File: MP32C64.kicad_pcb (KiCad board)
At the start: 2 copper layers, 14 parts, among them CN2 C64_CASS_PORT, SW1 SW_SPDT, U1 4069

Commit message: Almost ready
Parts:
- added CN1: AUDIO_IN, MP32C64:SWITCHCRAFT_PJRAN1X1U01X, F.Cu at (155.1, 94.7)
- R1, R2, R3, R4, R5, R6, R7, R8: footprint Resistor_THT:R_Axial_DIN0207_L6.3mm_D2.5mm_P7.62mm_Horizontal -> Resistor_THT:R_Axial_DIN0207_L6.3mm_D2.5mm_P10.16mm_Horizontal
- SW1: value SW_SPDT -> SW_INVERT
- U1: value 4069 -> CD4069
- moved SW1 49.3 mm to (136.0, 114.1)
- moved LD1 47.5 mm to (136.0, 98.8), turned to 90 degrees
- moved R7 44.7 mm to (136.0, 109.0), turned to 0 degrees
- moved R6 43.9 mm to (142.4, 91.2), turned to -90 degrees
- moved R8 43.2 mm to (139.8, 91.2), turned to -90 degrees
- moved R5 25.2 mm to (136.0, 106.4), turned to 0 degrees
- moved C2 23.6 mm to (158.9, 114.1), turned to -90 degrees
- moved R3 10.3 mm to (147.4, 101.3)
- moved R2 5.85 mm to (144.9, 101.3)
- moved R4 5.12 mm to (146.2, 103.9)
- moved C1 4.53 mm to (158.9, 109.0)
- moved U1 1.91 mm to (155.1, 112.8)
- moved R1 1.42 mm to (148.7, 103.9)
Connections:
- net /write renamed /write_1
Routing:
- net /motor: track 0.00 -> 35.5 mm, vias 0 -> 1
- net Net-(SW1-C): track 0.00 -> 21.4 mm
- net +5V: track 6.35 -> 26.6 mm, vias 0 -> 1
- net /read: track 13.7 -> 33.0 mm, vias 0 -> 1
- net Net-(R2-Pad1): track 17.3 -> 33.1 mm
- net Net-(R3-Pad1): track 8.67 -> 24.0 mm
- net Net-(SW1-A): track 17.5 -> 32.5 mm
- net Net-(LD1-A1): track 0.00 -> 10.3 mm
- net Net-(SW1-B): track 6.55 -> 14.5 mm
- net Net-(C1-Pad2): track 15.1 -> 21.2 mm
- net Net-(C1-Pad1): track 4.90 -> 10.5 mm
- net Net-(LD1-A2): track 0.00 -> 4.87 mm
- net GND: vias 0 -> 2
- added copper zone on B.Cu, net GND
- added copper zone on F.Cu, net GND
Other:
- board outline added: 31.4 x 41.9 mm
- board text added: "INV"
- board text added: "NORM"

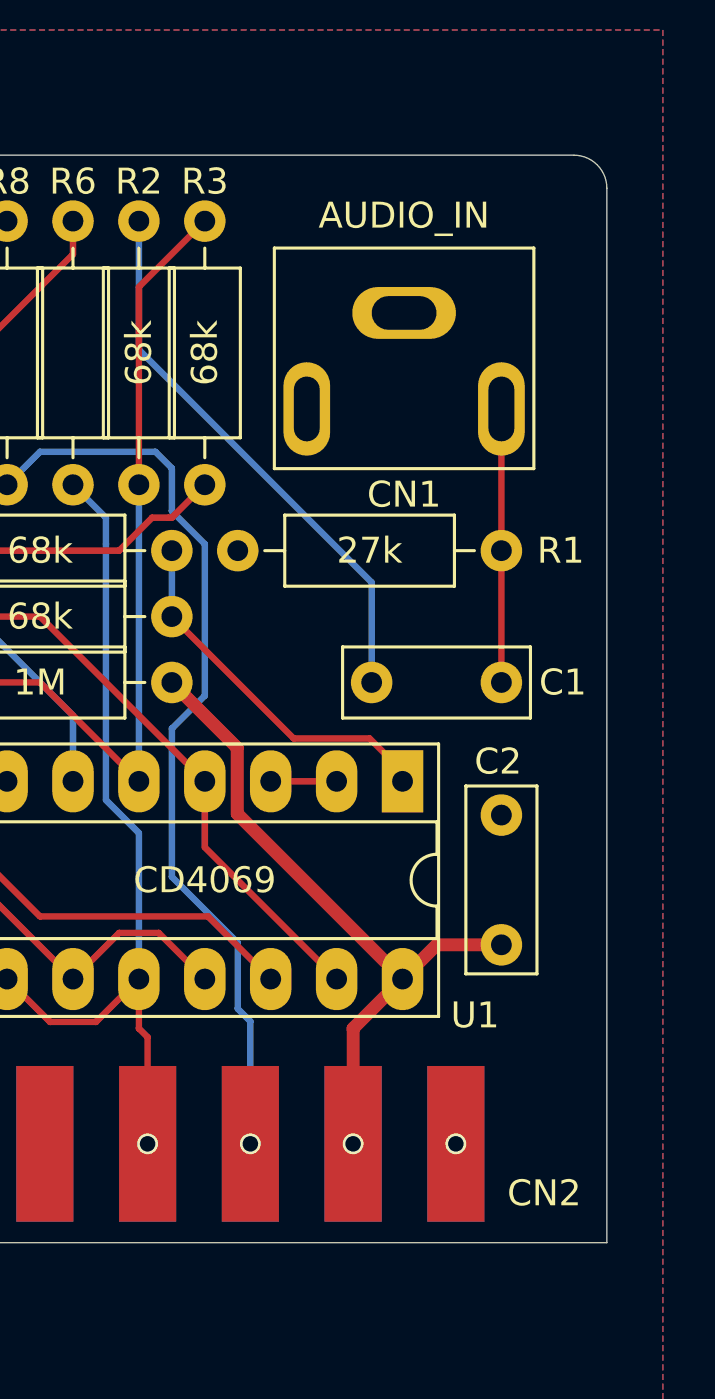
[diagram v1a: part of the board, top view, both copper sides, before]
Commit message: Add dual support for RCA/3.5" jack connector
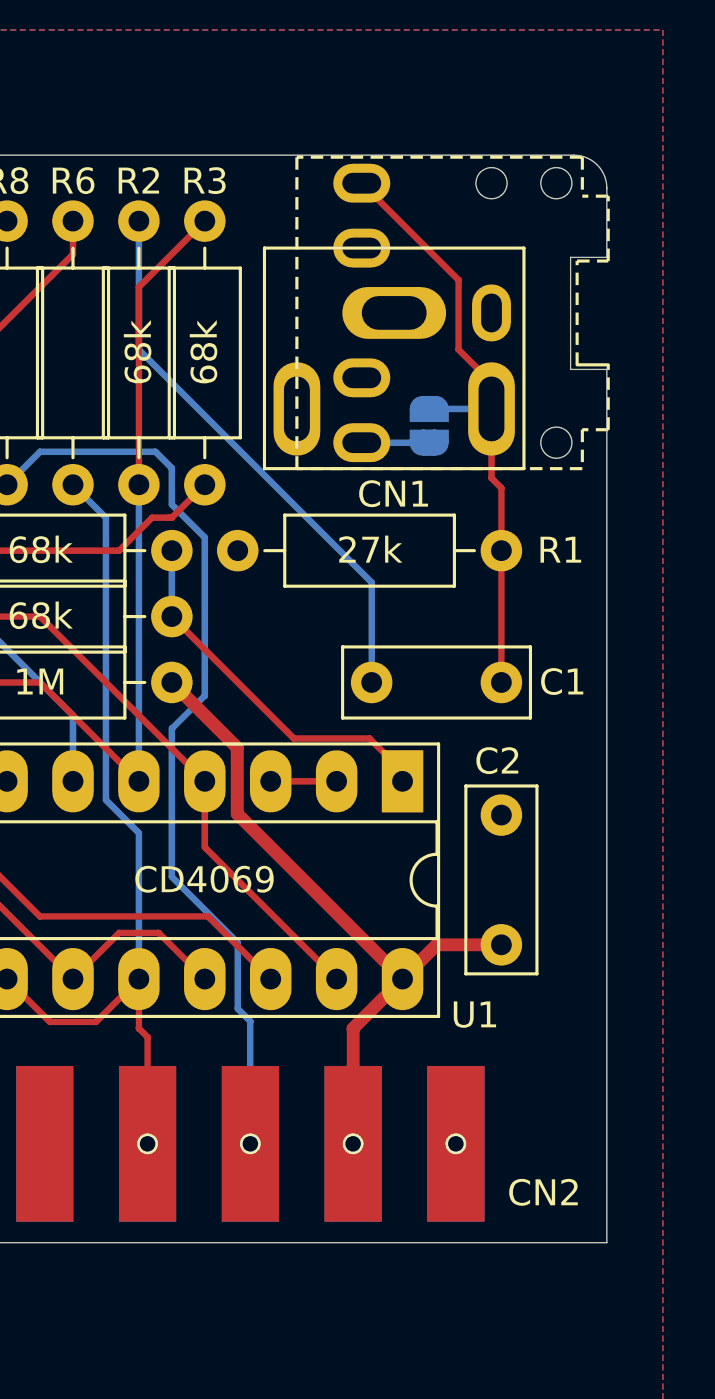
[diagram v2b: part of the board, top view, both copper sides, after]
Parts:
- added CNALT1: JACK_35IN, MP32C64:AudioJack_SJ1-3525N, F.Cu at (158.5, 94.7)
- added JP1: JMP_RING, Jumper:SolderJumper-2_P1.3mm_Open_RoundedPad1.0x1.5mm, B.Cu at (156.1, 99.1)
- moved CN1 0.38 mm to (154.7, 94.7)
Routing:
- net Net-(JP1-A): track 10.5 -> 23.9 mm
- net Net-(JP1-B): track 0.00 -> 2.63 mm
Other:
- outline, holes or cut-outs redrawn

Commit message: Add license, etc.
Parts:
- removed JP1: JMP_RING, Jumper:SolderJumper-2_P1.3mm_Open_RoundedPad1.0x1.5mm
- added V0: LICENSE, MP32C64:cc_by_nc_sa_small, B.Cu at (144.9, 94.3)
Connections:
- net /write_1 renamed /write
- CNALT1 pad R: Net-(JP1-B) -> unconnected-(CNALT1-PadR)
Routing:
- net Net-(JP1-B): track 2.63 -> 0.00 mm
- net Net-(C1-Pad1): track 23.9 -> 21.5 mm
- net /write: vias 0 -> 1
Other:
- board size 31.4 x 41.9 mm -> 31.4 x 41.8 mm
- board text added: "MP32C64 CC-BY-NC-SA"
- board text added: "Original design by Kopsec"
- board text added: "V1"
- board text added: "github.com/SukkoPera/ MP32C64"

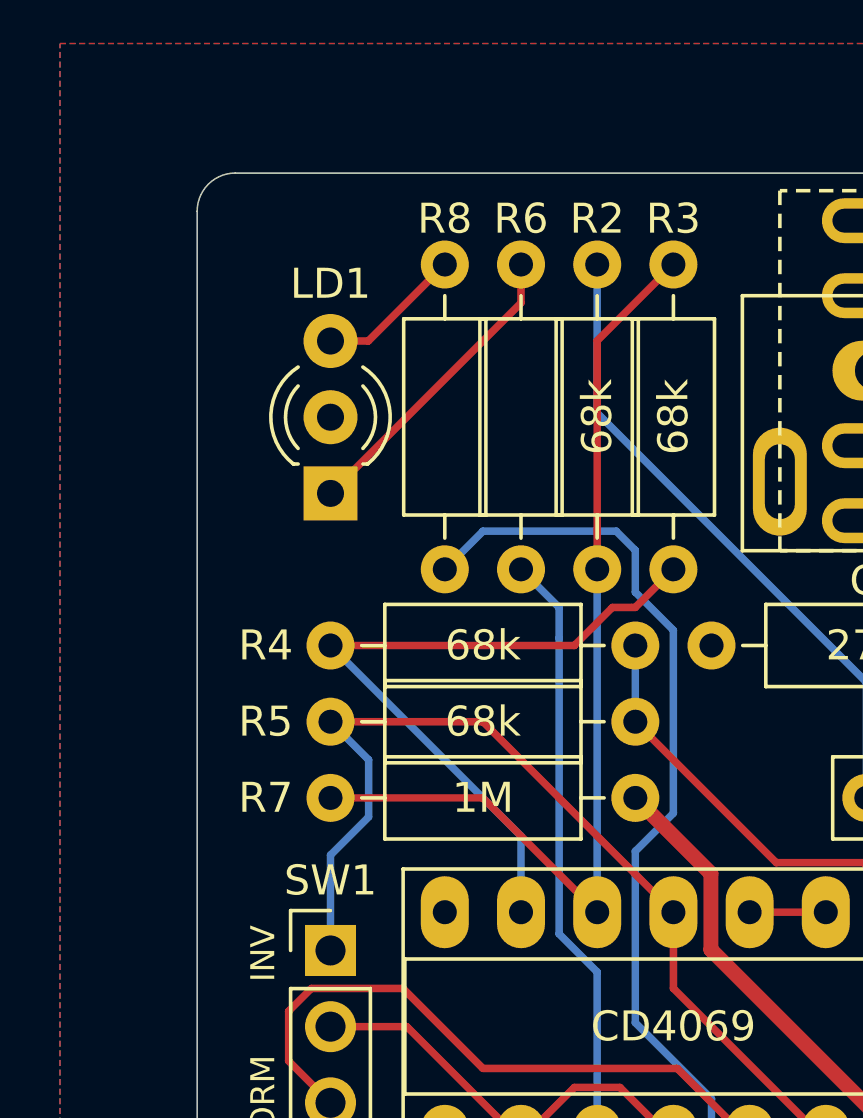
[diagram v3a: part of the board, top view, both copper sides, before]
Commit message: Replace dual LED with 2 separate LEDs
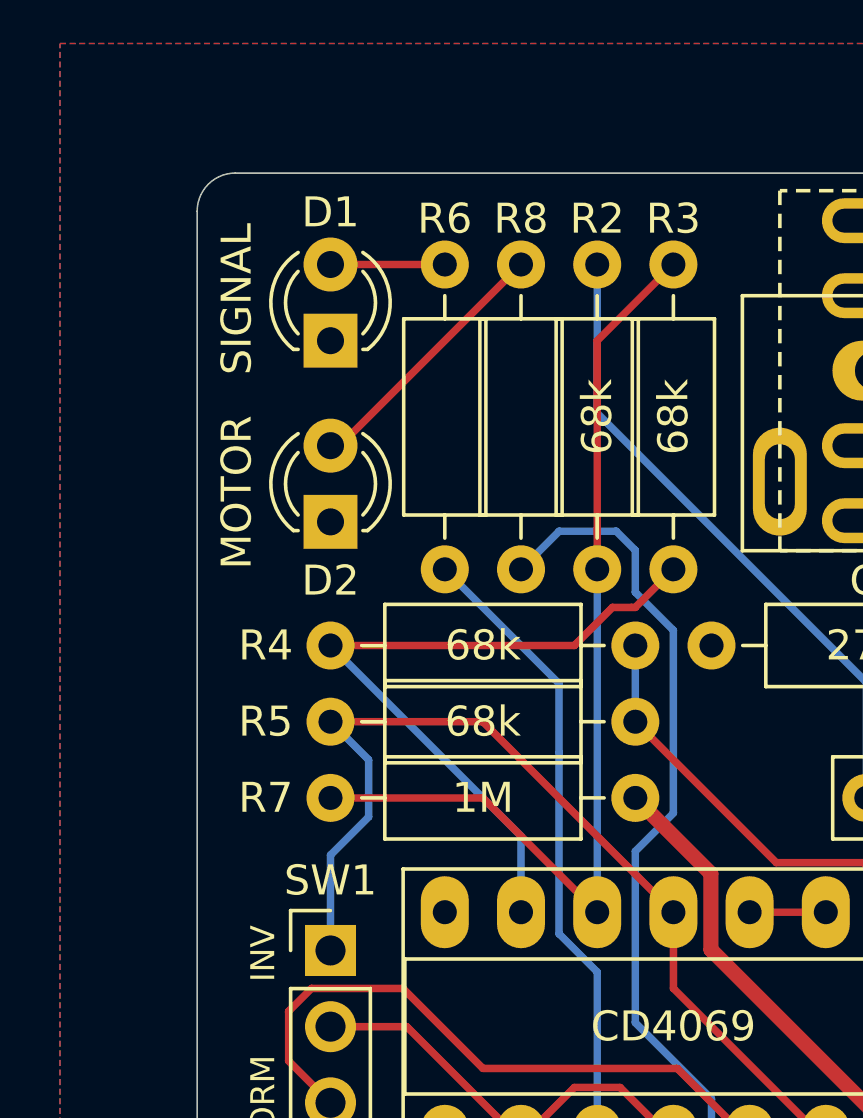
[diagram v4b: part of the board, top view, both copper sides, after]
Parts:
- removed LD1: LED, LED_THT:LED_D3.0mm-3
- added D1: LED_SIGNAL, LED_THT:LED_D3.0mm, F.Cu at (136.0, 93.7)
- added D2: LED_MOTOR, LED_THT:LED_D3.0mm, F.Cu at (136.0, 99.8)
- moved R6 2.54 mm to (139.8, 91.2)
- moved R8 2.54 mm to (142.4, 91.2)
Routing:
- net Net-(D1-A): track 10.3 -> 3.81 mm
- net Net-(D2-A): track 4.87 -> 8.85 mm
- net /motor: track 35.5 -> 32.9 mm
- net /read: track 33.0 -> 34.1 mm
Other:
- board text added: "MOTOR"
- board text added: "SIGNAL"

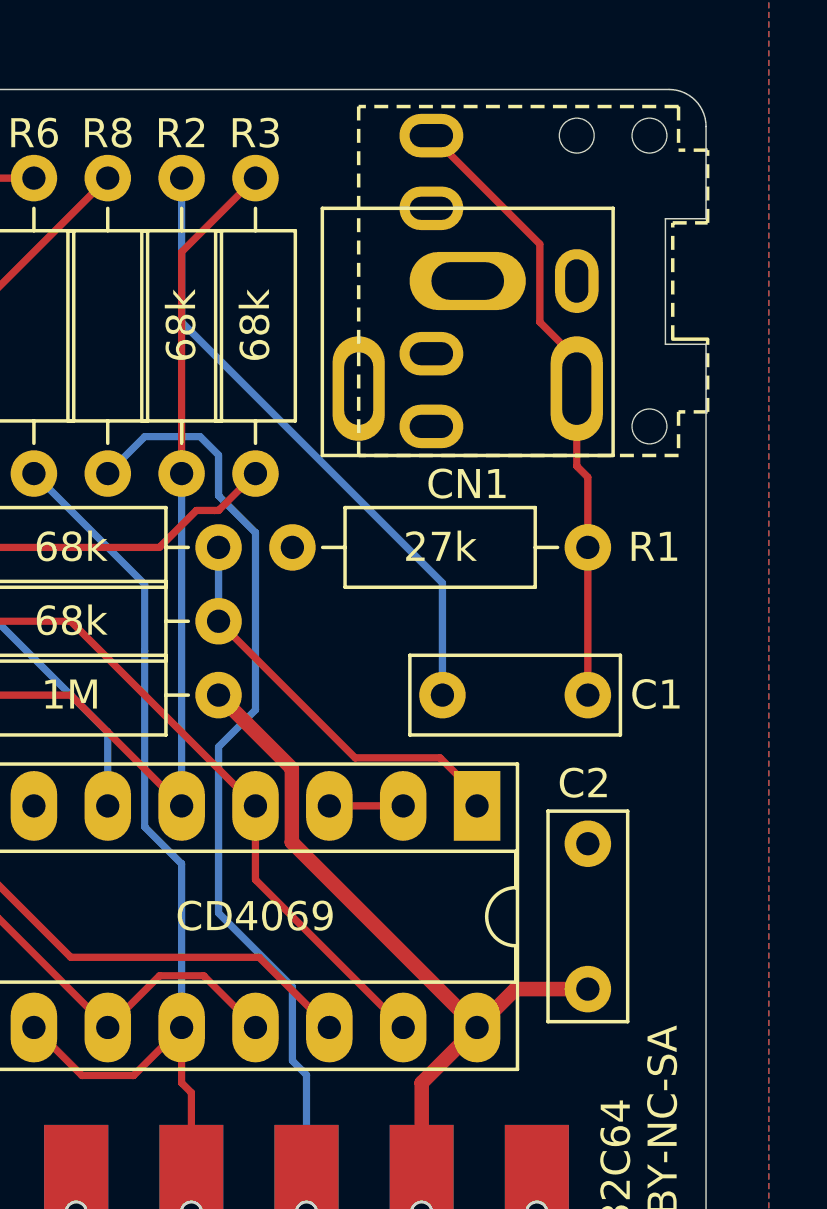
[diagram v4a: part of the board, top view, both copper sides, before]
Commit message: Add C2, found in some other schematics
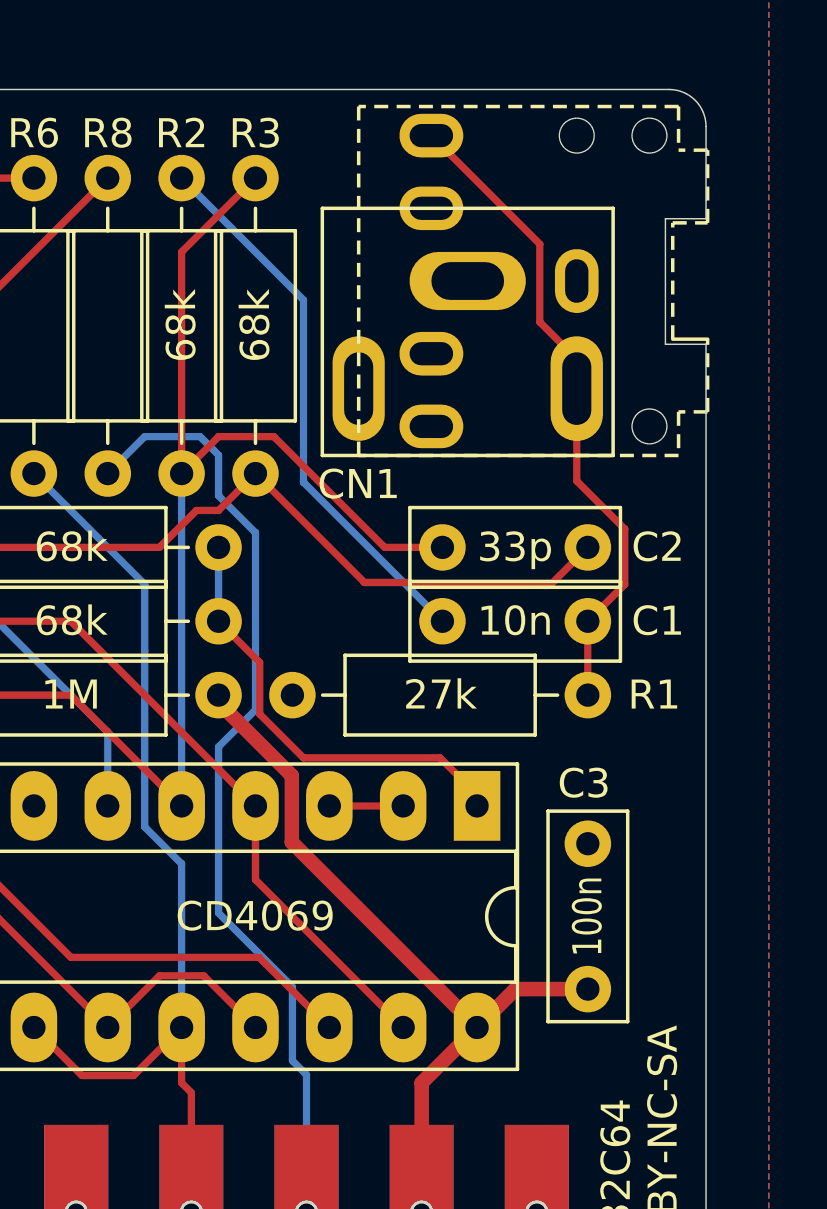
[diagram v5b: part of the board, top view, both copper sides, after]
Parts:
- added C2: 33p, Capacitor_THT:C_Disc_D7.0mm_W2.5mm_P5.00mm, F.Cu at (153.9, 103.9)
- moved R1 5.08 mm to (148.7, 109.0)
- moved C1 2.54 mm to (158.9, 106.4)
- renumbered C2 to C3
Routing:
- net Net-(C2-Pad2): track 24.0 -> 37.5 mm
- net Net-(C2-Pad1): track 33.1 -> 44.2 mm
- net Net-(C1-Pad2): track 21.2 -> 19.0 mm
- net Net-(C1-Pad1): track 21.5 -> 22.5 mm
- net Net-(R4-Pad1): track 13.6 -> 14.7 mm

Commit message: Tidy up
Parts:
- moved C1 2.58 mm to (156.3, 106.4)
- moved C2 2.42 mm to (156.3, 103.9), turned to 180 degrees
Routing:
- net Net-(C2-Pad2): track 37.5 -> 28.9 mm
- net Net-(C2-Pad1): track 44.2 -> 47.1 mm
- net Net-(C1-Pad2): track 19.0 -> 17.9 mm
- net Net-(C1-Pad1): track 22.5 -> 23.3 mm

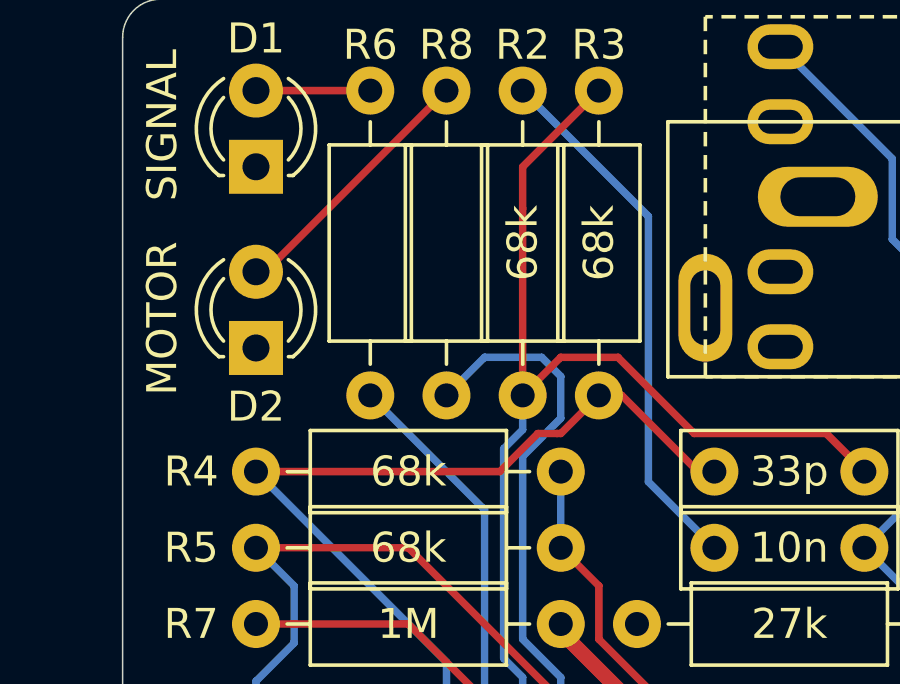
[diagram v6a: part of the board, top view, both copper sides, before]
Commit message: Fix resistor values & add renders
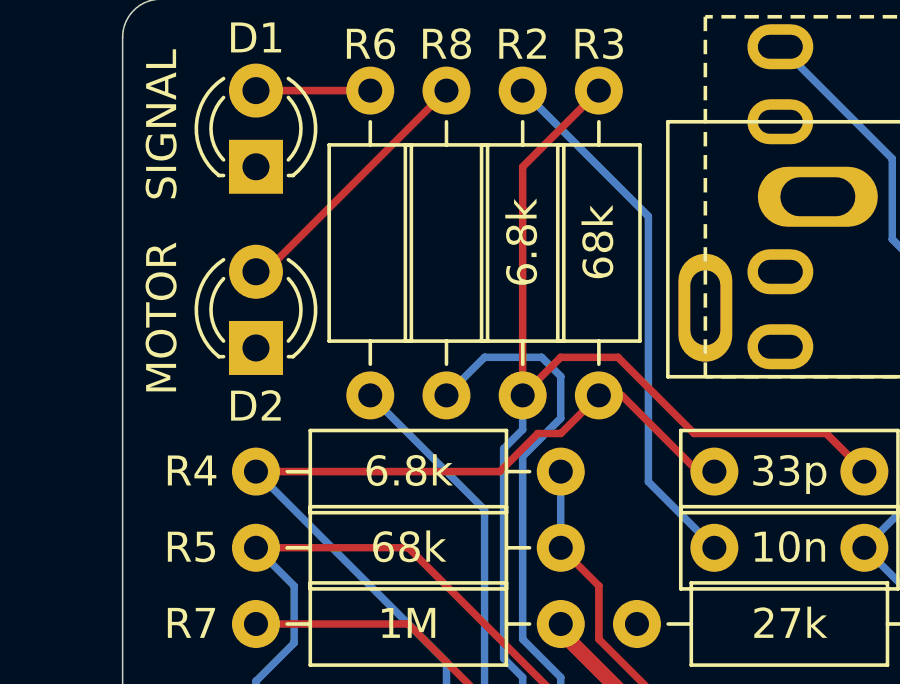
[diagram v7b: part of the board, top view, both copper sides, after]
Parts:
- R2, R4: value 68k -> 6.8k
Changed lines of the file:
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@@
 			)
 		)
-		(property "Value" "68k"
+		(property "Value" "6.8k"
 			(at 5.08 0 90)
 			(layer "F.SilkS")
@@
 			)
 		)
-		(property "Value" "68k"
+		(property "Value" "6.8k"
 			(at 5.08 0 180)
 			(layer "F.SilkS")
